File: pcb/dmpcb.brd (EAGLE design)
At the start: 160 x 100 mm, 41 parts, among them IC1 7805DT, IC2 L293D, IC3 MAX7219CNG, Q1 IRF530, Q2 IRF530

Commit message: Holy hell, I have no idea what I am doing. This is so different from kicad. brb, gone to watch tutorials....
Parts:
- moved U$1 64.4 mm to (41.9, 12.7), turned to 180 degrees
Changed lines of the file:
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@@
 <attribute name="VALUE" x="-19.05" y="61.976" size="0.6096" layer="27" font="vector" ratio="20"/>
 </element>
-<element name="U$1" library="Teensy3.1_ralfsfix" package="TEENSY3.1_ALL_RALF" value="TEENSY3.1_ALL" x="-20.32" y="29.21" smashed="yes"/>
+<element name="U$1" library="Teensy3.1_ralfsfix" package="TEENSY3.1_ALL_RALF" value="TEENSY3.1_ALL" x="41.91" y="12.7" smashed="yes" rot="R180"/>
 </elements>
 <signals>
@@
 <wire x1="-50.8" y1="3.81" x2="-64.77" y2="8.85" width="0" layer="19" extent="1-1"/>
 <wire x1="-39.37" y1="3.81" x2="-50.8" y2="3.81" width="0" layer="19" extent="1-1"/>
-<wire x1="-25.4" y1="6.35" x2="-39.37" y2="3.81" width="0" layer="19" extent="1-1"/>
-<wire x1="-25.4" y1="21.59" x2="-25.4" y2="6.35" width="0" layer="19" extent="1-1"/>
-<wire x1="-33.02" y1="39.37" x2="-25.4" y2="21.59" width="0" layer="19" extent="1-1"/>
-<wire x1="-34.29" y1="43.18" x2="-33.02" y2="39.37" width="0" layer="19" extent="1-1"/>
-<wire x1="-21.59" y1="43.18" x2="-33.02" y2="39.37" width="0" layer="19" extent="1-1"/>
+<wire x1="46.99" y1="35.56" x2="-39.37" y2="3.81" width="0" layer="19" extent="1-1"/>
+<wire x1="46.99" y1="20.32" x2="46.99" y2="35.56" width="0" layer="19" extent="1-1"/>
+<wire x1="54.61" y1="2.54" x2="46.99" y2="20.32" width="0" layer="19" extent="1-1"/>
+<wire x1="-34.29" y1="43.18" x2="54.61" y2="2.54" width="0" layer="19" extent="1-1"/>
+<wire x1="-21.59" y1="43.18" x2="54.61" y2="2.54" width="0" layer="19" extent="1-1"/>
 <wire x1="-55.88" y1="43.18" x2="-34.29" y2="43.18" width="0" layer="19" extent="1-1"/>
 <wire x1="-58.42" y1="43.18" x2="-55.88" y2="43.18" width="0" layer="19" extent="1-1"/>
@@
 <wire x1="-62.45" y1="78.74" x2="-48.78" y2="73.66" width="0" layer="19" extent="1-1"/>
 <wire x1="-29.21" y1="50.8" x2="-40.31" y2="66.04" width="0" layer="19" extent="1-1"/>
-<wire x1="-17.78" y1="39.37" x2="-29.21" y2="50.8" width="0" layer="19" extent="1-1"/>
+<wire x1="39.37" y1="2.54" x2="-29.21" y2="50.8" width="0" layer="19" extent="1-1"/>
 <wire x1="-66.04" y1="50.8" x2="-62.45" y2="78.74" width="0" layer="19" extent="1-1"/>
 <wire x1="-62.49" y1="1.55" x2="-66.04" y2="50.8" width="0" layer="19" extent="1-1"/>
@@
 <contactref element="R6" pad="1"/>
 <contactref element="U$1" pad="D3"/>
-<wire x1="-33.02" y1="29.21" x2="-31.43" y2="80.01" width="0" layer="19" extent="1-1"/>
+<wire x1="54.61" y1="12.7" x2="-31.43" y2="80.01" width="0" layer="19" extent="1-1"/>
 </signal>
 <signal name="N$5">
@@
 <contactref element="IC2" pad="1"/>
 <contactref element="U$1" pad="D8"/>
-<wire x1="-33.02" y1="16.51" x2="-66.04" y2="43.18" width="0" layer="19" extent="1-1"/>
+<wire x1="54.61" y1="25.4" x2="-66.04" y2="43.18" width="0" layer="19" extent="1-1"/>
 </signal>
 <signal name="L293IN01">
 <contactref element="IC2" pad="2"/>
 <contactref element="U$1" pad="D6"/>
-<wire x1="-33.02" y1="21.59" x2="-63.5" y2="43.18" width="0" layer="19" extent="1-1"/>
+<wire x1="54.61" y1="20.32" x2="-63.5" y2="43.18" width="0" layer="19" extent="1-1"/>
 </signal>
 <signal name="N$8">
@@
 <contactref element="R2" pad="1"/>
 <contactref element="U$1" pad="D2"/>
-<wire x1="-33.02" y1="31.75" x2="-26.35" y2="80.01" width="0" layer="19" extent="1-1"/>
+<wire x1="54.61" y1="10.16" x2="-26.35" y2="80.01" width="0" layer="19" extent="1-1"/>
 </signal>
 <signal name="POT1">
@@
 <contactref element="R8" pad="1"/>
 <wire x1="-44.45" y1="3.81" x2="-55.88" y2="3.81" width="0" layer="19" extent="1-1"/>
-<wire x1="-27.94" y1="6.35" x2="-44.45" y2="3.81" width="0" layer="19" extent="1-1"/>
-<wire x1="-22.86" y1="21.59" x2="-27.94" y2="6.35" width="0" layer="19" extent="1-1"/>
-<wire x1="-17.78" y1="34.29" x2="-22.86" y2="21.59" width="0" layer="19" extent="1-1"/>
+<wire x1="49.53" y1="35.56" x2="-44.45" y2="3.81" width="0" layer="19" extent="1-1"/>
+<wire x1="44.45" y1="20.32" x2="49.53" y2="35.56" width="0" layer="19" extent="1-1"/>
+<wire x1="39.37" y1="7.62" x2="44.45" y2="20.32" width="0" layer="19" extent="1-1"/>
 </signal>
 <signal name="DNC">
@@
 <wire x1="-17.78" y1="58.42" x2="-15.24" y2="58.42" width="0" layer="19" extent="1-1"/>
 <wire x1="-20.32" y1="58.42" x2="-17.78" y2="58.42" width="0" layer="19" extent="1-1"/>
-<wire x1="-33.02" y1="13.97" x2="-20.32" y2="58.42" width="0" layer="19" extent="1-1"/>
+<wire x1="54.61" y1="27.94" x2="-20.32" y2="58.42" width="0" layer="19" extent="1-1"/>
 </signal>
 <signal name="BUTTON01">
@@
 <wire x1="-54.0512" y1="53.6194" x2="-65.09" y2="73.66" width="0" layer="19" extent="1-1"/>
 <wire x1="-47.5488" y1="53.6194" x2="-54.0512" y2="53.6194" width="0" layer="19" extent="1-1"/>
-<wire x1="-33.02" y1="26.67" x2="-47.5488" y2="53.6194" width="0" layer="19" extent="1-1"/>
+<wire x1="54.61" y1="15.24" x2="-47.5488" y2="53.6194" width="0" layer="19" extent="1-1"/>
 </signal>
 <signal name="BUTTON02">
@@
 <wire x1="-57.7088" y1="53.6194" x2="-64.2112" y2="53.6194" width="0" layer="19" extent="1-1"/>
 <wire x1="-70.17" y1="73.66" x2="-64.2112" y2="53.6194" width="0" layer="19" extent="1-1"/>
-<wire x1="-33.02" y1="24.13" x2="-57.7088" y2="53.6194" width="0" layer="19" extent="1-1"/>
+<wire x1="54.61" y1="17.78" x2="-57.7088" y2="53.6194" width="0" layer="19" extent="1-1"/>
 </signal>
 <signal name="AUDIOOUT">
@@
 <contactref element="IC3" pad="13"/>
 <contactref element="U$1" pad="D12"/>
-<wire x1="-33.02" y1="6.35" x2="-13.97" y2="50.8" width="0" layer="19" extent="1-1"/>
+<wire x1="54.61" y1="35.56" x2="-13.97" y2="50.8" width="0" layer="19" extent="1-1"/>
 </signal>
 <signal name="MAX7219LOAD">
 <contactref element="IC3" pad="12"/>
 <contactref element="U$1" pad="D11"/>
-<wire x1="-33.02" y1="8.89" x2="-13.97" y2="43.18" width="0" layer="19" extent="1-1"/>
+<wire x1="54.61" y1="33.02" x2="-13.97" y2="43.18" width="0" layer="19" extent="1-1"/>
 </signal>
 <signal name="MAX7219DIN">
 <contactref element="IC3" pad="1"/>
 <contactref element="U$1" pad="D10"/>
-<wire x1="-41.91" y1="43.18" x2="-33.02" y2="11.43" width="0" layer="19" extent="1-1"/>
+<wire x1="-41.91" y1="43.18" x2="54.61" y2="30.48" width="0" layer="19" extent="1-1"/>
 </signal>
 <signal name="N$29">
@@
 <contactref element="IC2" pad="7"/>
 <contactref element="U$1" pad="D7"/>
-<wire x1="-50.8" y1="43.18" x2="-33.02" y2="19.05" width="0" layer="19" extent="1-1"/>
+<wire x1="-50.8" y1="43.18" x2="54.61" y2="22.86" width="0" layer="19" extent="1-1"/>
 </signal>
 <signal name="POT01">
 <contactref element="U$1" pad="A11"/>
 <contactref element="R7" pad="3"/>
-<wire x1="-20.32" y1="26.67" x2="-41.91" y2="13.97" width="0" layer="19" extent="1-1"/>
+<wire x1="41.91" y1="15.24" x2="-41.91" y2="13.97" width="0" layer="19" extent="1-1"/>
 </signal>
 <signal name="N$32">
@@
 <contactref element="R8" pad="3"/>
 <contactref element="U$1" pad="A10"/>
-<wire x1="-20.32" y1="29.21" x2="-53.34" y2="13.97" width="0" layer="19" extent="1-1"/>
+<wire x1="41.91" y1="12.7" x2="-53.34" y2="13.97" width="0" layer="19" extent="1-1"/>
 </signal>
 <signal name="N$25">

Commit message: don´t know what changed. well...
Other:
- board size 160 x 100 mm -> 99.1 x 100.3 mm
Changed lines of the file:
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@@
 <setting verticaltext="up"/>
 </settings>
-<grid distance="50" unitdist="mil" unit="mil" style="lines" multiple="1" display="no" altdistance="5" altunitdist="mil" altunit="mil"/>
+<grid distance="50" unitdist="mil" unit="mm" style="lines" multiple="1" display="no" altdistance="5" altunitdist="mil" altunit="mm"/>
 <layers>
 <layer number="1" name="Top" color="4" fill="1" visible="yes" active="yes"/>
@@
 <layer number="43" name="vRestrict" color="2" fill="10" visible="yes" active="yes"/>
 <layer number="44" name="Drills" color="7" fill="1" visible="no" active="yes"/>
-<layer number="45" name="Holes" color="7" fill="1" visible="no" active="yes"/>
+<layer number="45" name="Holes" color="7" fill="1" visible="yes" active="yes"/>
 <layer number="46" name="Milling" color="3" fill="1" visible="no" active="yes"/>
 <layer number="47" name="Measures" color="7" fill="1" visible="no" active="yes"/>
@@
 <board>
 <plain>
-<wire x1="0" y1="0" x2="160" y2="0" width="0" layer="20"/>
-<wire x1="160" y1="0" x2="160" y2="100" width="0" layer="20"/>
-<wire x1="160" y1="100" x2="0" y2="100" width="0" layer="20"/>
 <wire x1="0" y1="100" x2="0" y2="0" width="0" layer="20"/>
+<wire x1="0" y1="0" x2="99.06" y2="0" width="0.1524" layer="20"/>
+<wire x1="99.06" y1="0" x2="99.06" y2="100.33" width="0.1524" layer="20"/>
+<wire x1="99.06" y1="100.33" x2="0" y2="100.33" width="0.1524" layer="20"/>
+<wire x1="0" y1="100.33" x2="0" y2="0" width="0.1524" layer="20"/>
 </plain>
 <attributes>

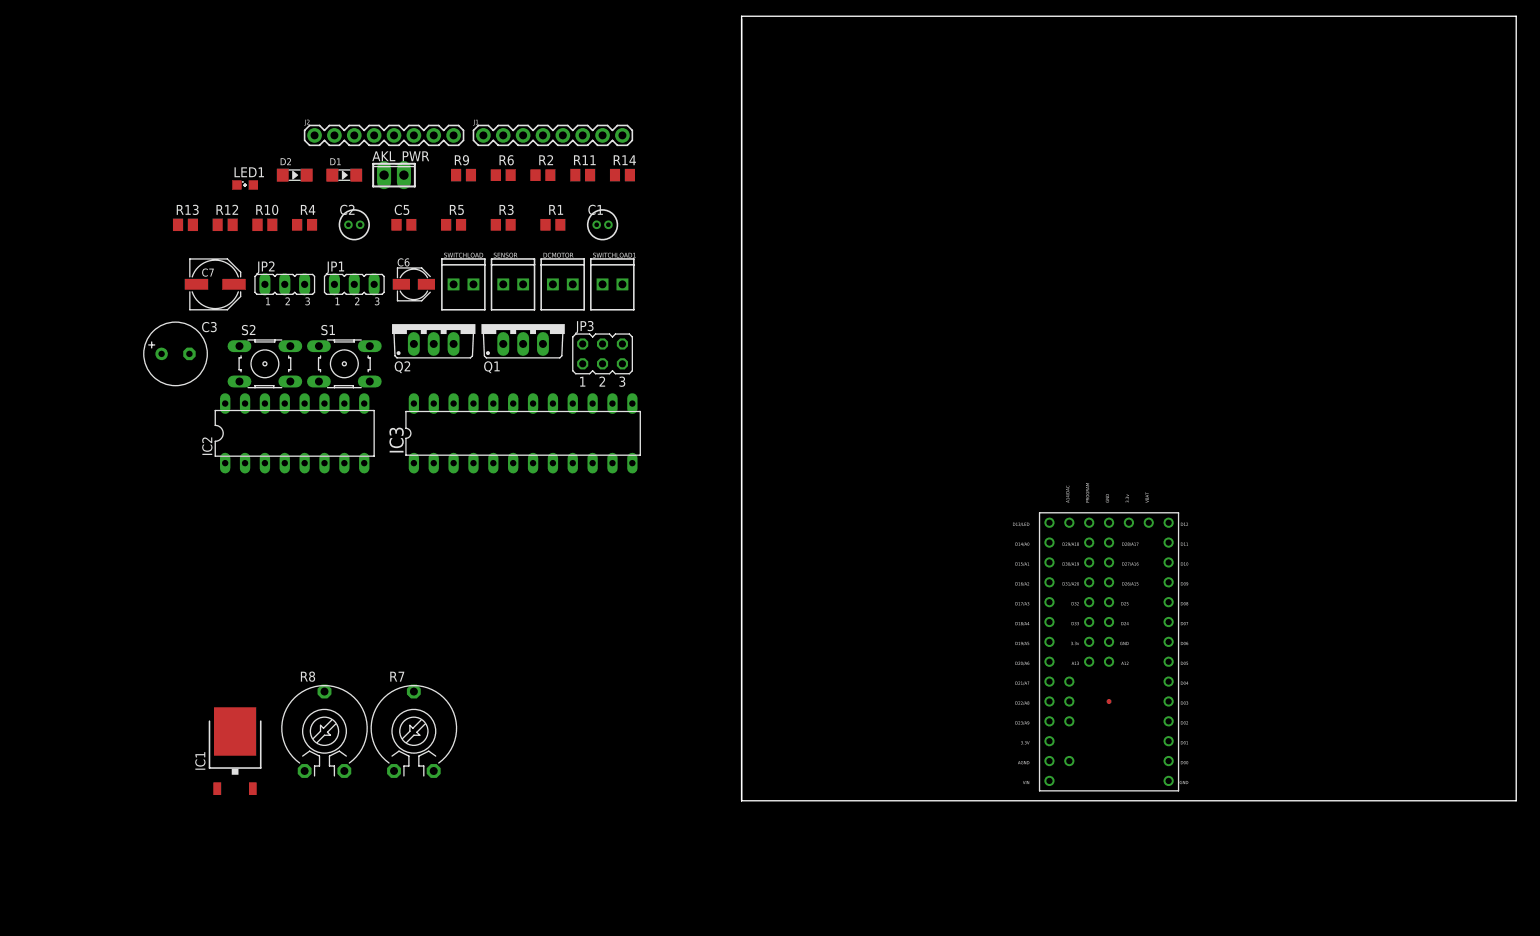
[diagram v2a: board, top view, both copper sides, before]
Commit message: found footprint for drv8825 carrier board, included it into schematic
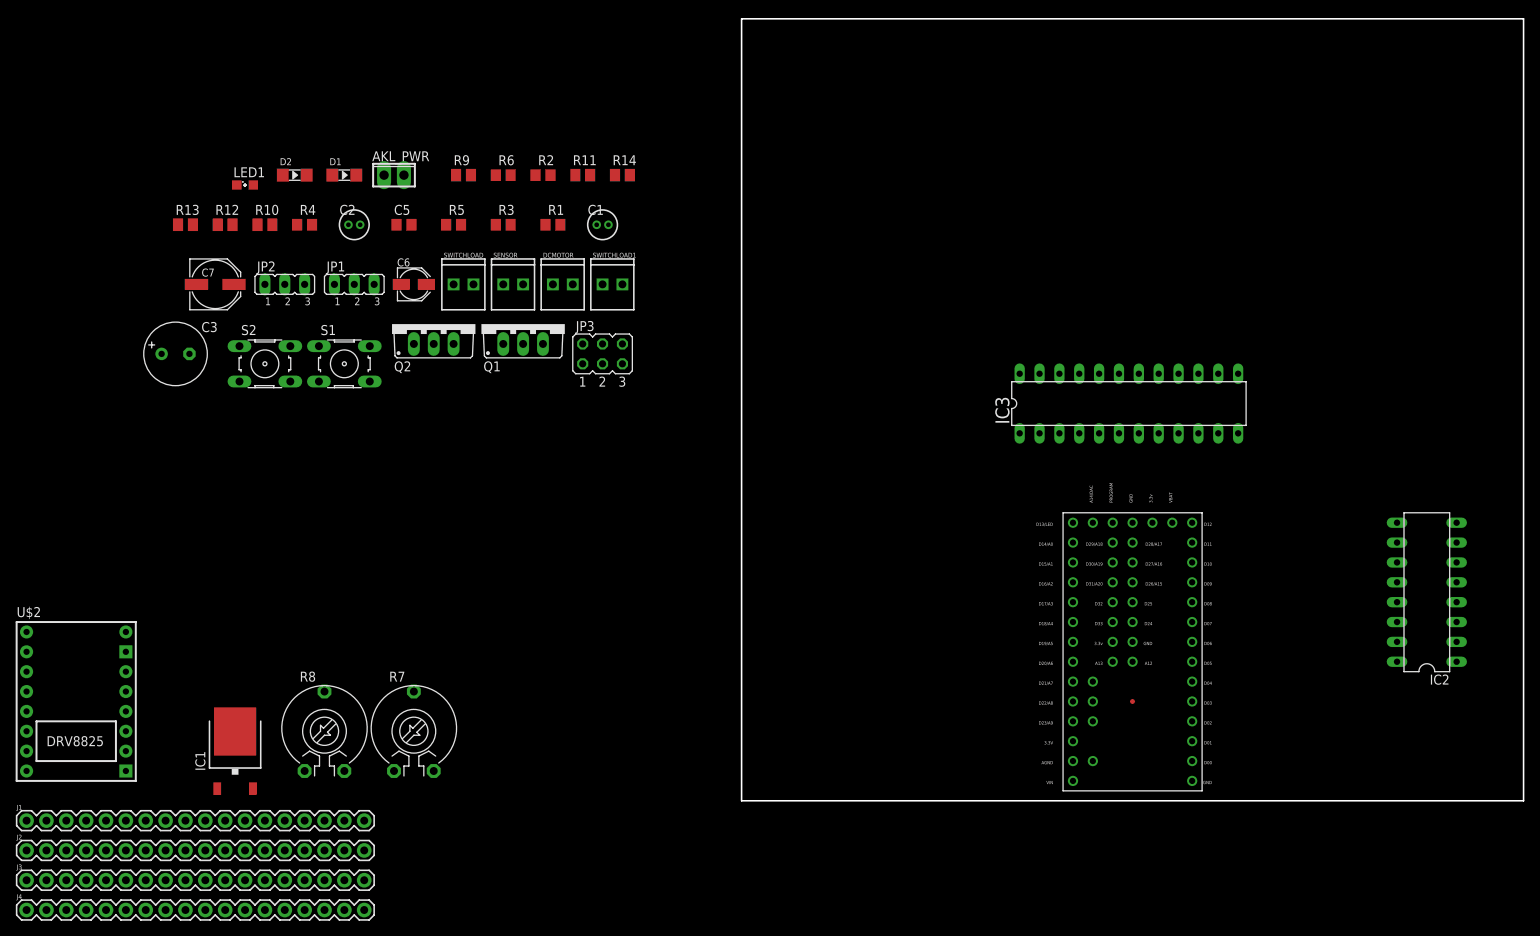
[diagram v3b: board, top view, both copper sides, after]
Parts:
- added J3, J4: (no value), SparkFun-Connectors:1X18
- added U$2: POLOLU-DRV8825, alvarop-lib:POLOLU-DRV8825
- J1, J2: device SparkFun-Connectors:1X08 -> SparkFun-Connectors:1X18
- moved IC2 146.2 mm to (87.6, 26.7), turned to 90 degrees
- moved J1 105.3 mm to (-91.4, -2.54)
- moved J2 98.6 mm to (-91.4, -6.35)
- moved IC3 77.6 mm to (49.5, 50.8)
- moved U$1 3.01 mm to (44.9, 12.7)
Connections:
- removed net COIL1A: J2.4
- removed net COIL1B: J2.5
- removed net COIL2A: J2.3
- removed net COIL2B: J2.6
- new net A1: U$2.A1
- new net A2: U$2.A2
- new net B1: U$2.B1
- new net B2: U$2.B2
- net DIR: now also U$2.DIR; no longer J1.8
- net DNC: now also U$2.FLT_N; no longer J2.2
- net EN: now also U$2.EN_N; no longer J1.1
- net GND: now also U$2.GND, U$2.GND2; no longer J2.1, J2.7
- net M0: now also U$2.M0; no longer J1.2
- net M1: now also U$2.M1; no longer J1.3
- net M2: now also U$2.M2; no longer J1.4
- net RST: now also U$2.RST_N; no longer J1.5
- net SLP: now also U$2.SLP_N; no longer J1.6
- net STP: now also U$2.STEP_N; no longer J1.7
- net VMOT: now also U$2.VMOT; no longer J2.8
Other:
- board size 99.1 x 100.3 mm -> 100 x 100 mm
